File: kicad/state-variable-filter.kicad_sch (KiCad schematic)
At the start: 107 parts, among them J1 AudioJack2_SwitchT, J10 AudioJack2_SwitchT, J11 AudioJack2_SwitchT, J12 Conn_01x08_Pin, J13 Conn_01x08_Socket, J14 Conn_01x08_Pin, J15 Conn_02x05_Odd_Even, J2 Conn_01x08_Socket, J3 AudioJack2_SwitchT, J4 AudioJack2_SwitchT, J5 AudioJack2_SwitchT, J6 AudioJack2_SwitchT, J7 AudioJack2_SwitchT, J8 AudioJack2_SwitchT, J9 AudioJack2_SwitchT, U1 TL072, U2 TL074, U3 SSI2164, U4 TL074

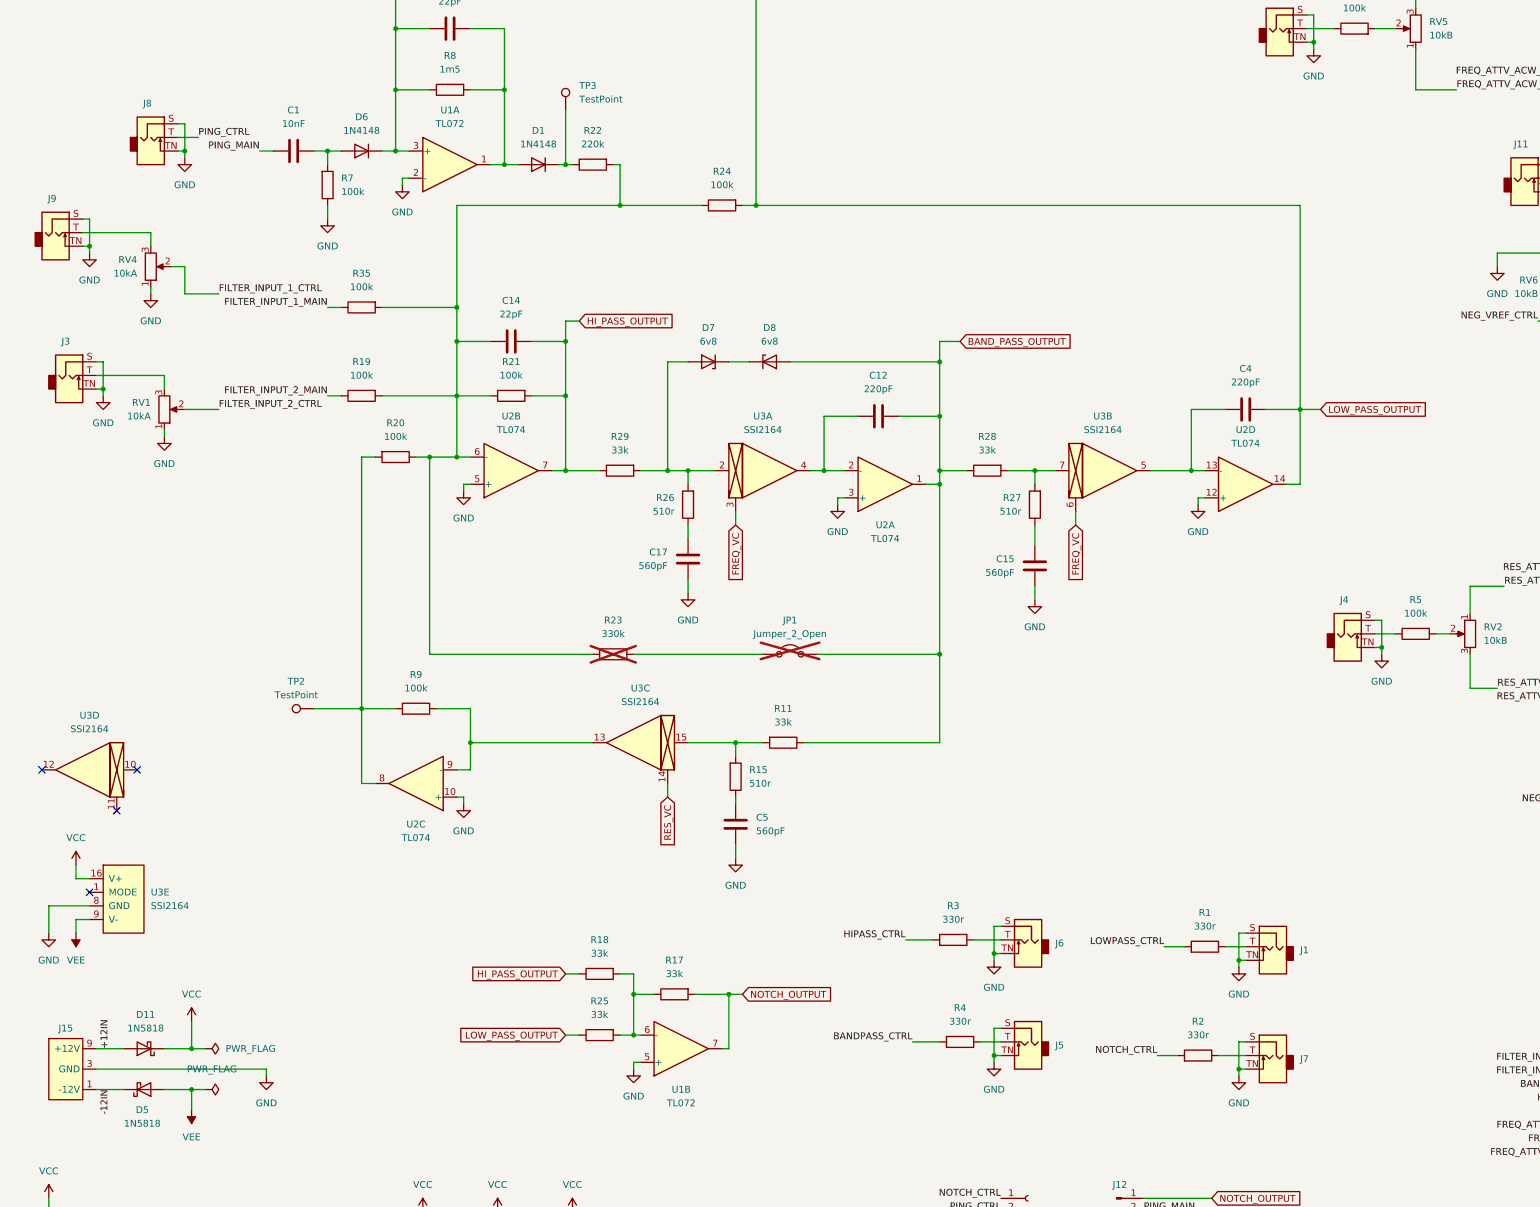
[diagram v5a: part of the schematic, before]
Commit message: Updating with rev02 fixes
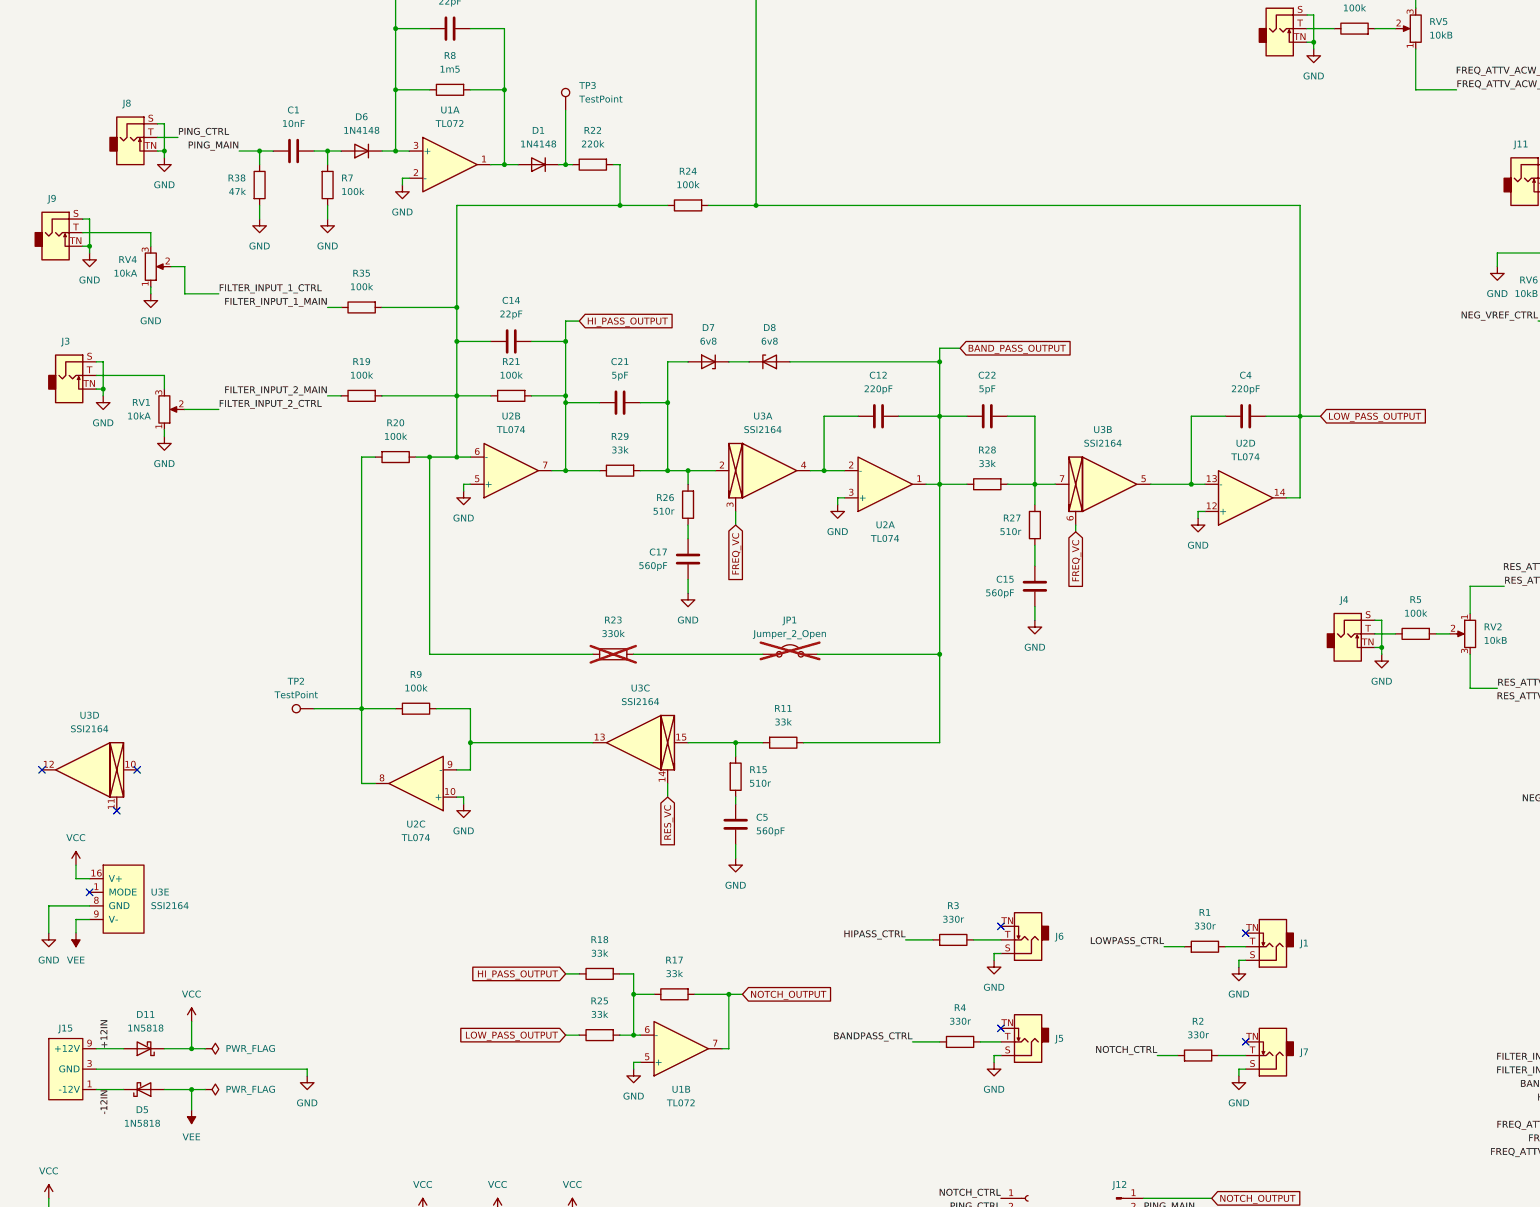
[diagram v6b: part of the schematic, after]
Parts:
- added C21, C22: 5pF, Rumblesan_Standard_Parts:C_Rect_L7.0mm_W2.5mm_P5.00mm, symbol Rumblesan_Standard_Parts:C
- added R38: 47k, Rumblesan_Standard_Parts:R_Axial_DIN0207_L6.3mm_D2.5mm_P10.16mm_Horizontal, symbol Rumblesan_Standard_Parts:R
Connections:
- net BAND_PASS_OUTPUT: now also C22.1
- net GND: now also R38.1; no longer J1.TN, J5.TN, J6.TN, J7.TN
- net HI_PASS_OUTPUT: now also C21.1
- net PING_MAIN: now also R38.2
- net at D7.2 (A), R26.1, R29.1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: now also C21.2
- net at R27.1, R28.1, U3.7: now also C22.2
- no-connect marks 4 -> 8
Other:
- company: (none) -> Bristol Communal Modular
- title: (none) -> 2164 State Variable Filter
- moved on the sheet: C15, C4, J1, J5, J6, J7, J8, R24, R27, R28, U2D, U3B
